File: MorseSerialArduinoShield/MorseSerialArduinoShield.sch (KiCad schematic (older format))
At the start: 13 parts, among them P1 Power, P2 Analog, P3 Digital, P4 Digital, P5 CONN_01X01, P6 CONN_01X01, P7 CONN_01X01, P8 CONN_01X01

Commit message: Organised project
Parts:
- added R? (x7): 1K, symbol Device:R
- R?: value R -> 1K
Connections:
- net at U?.1 (G): now also R?.1
- net at U?.10 (A): now also R?.1
- net at U?.2 (F): now also R?.1
- net at U?.4 (E): now also R?.1
- net at U?.5 (D): now also R?.1
- net at U?.6 (DP): now also R?.1
- net at U?.7 (C): now also R?.1
- net at U?.9 (B): now also R?.1
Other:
- note added: "pinMode(2, OUTPUT); // top right\n pinMode(4, OUTPUT); // top left\n pinMode(5, OUTPUT); // top centre\n pinMode(6, OUTPUT); // middle\n pinMode(7, OUTPUT); // Decimal point\n pinMode(8, OUTPUT); // bottom Right\n pinMode(10, OUTPUT); // bottom left\n pinMode(11, OUTPUT); // bottom\n pinMode(13, OUTPUT); // Buzzer"
- moved on the sheet: A?, BZ?, R?, RV?, U?
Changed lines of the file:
@@
 L Device:Buzzer BZ?
 U 1 1 5E8A2230
-P 4550 3100
-F 0 "BZ?" H 4702 3129 50  0000 L CNN
-F 1 "Buzzer" H 4702 3038 50  0000 L CNN
-F 2 "" V 4525 3200 50  0001 C CNN
-F 3 "~" V 4525 3200 50  0001 C CNN
-	1    4550 3100
-	1    0    0    -1
+P 4100 750
+F 0 "BZ?" H 4252 779 50  0000 L CNN
+F 1 "Buzzer" H 4252 688 50  0000 L CNN
+F 2 "" V 4075 850 50  0001 C CNN
+F 3 "~" V 4075 850 50  0001 C CNN
+	1    4100 750
+	0    -1   -1   0
 $EndComp
 $Comp
 L Display_Character:SC39-11SRWA U?
 U 1 1 5E8A0889
-P 4550 1850
-F 0 "U?" H 4550 2517 50  0000 C CNN
-F 1 "SC39-11SRWA" H 4550 2426 50  0000 C CNN
-F 2 "Display_7Segment:Sx39-1xxxxx" H 4550 1300 50  0001 C CNN
-F 3 "http://www.kingbrightusa.com/images/catalog/SPEC/sc39-11srwa.pdf" H 4550 1850 50  0001 C CNN
-	1    4550 1850
+P 4950 2300
+F 0 "U?" H 4950 2967 50  0000 C CNN
+F 1 "SC39-11SRWA" H 4950 2876 50  0000 C CNN
+F 2 "Display_7Segment:Sx39-1xxxxx" H 4950 1750 50  0001 C CNN
+F 3 "http://www.kingbrightusa.com/images/catalog/SPEC/sc39-11srwa.pdf" H 4950 2300 50  0001 C CNN
+	1    4950 2300
 	1    0    0    -1
 $EndComp
@@
 L Device:R R?
 U 1 1 5E8A1C48
-P 5600 2450
-F 0 "R?" H 5670 2496 50  0000 L CNN
-F 1 "R" H 5670 2405 50  0000 L CNN
-F 2 "" V 5530 2450 50  0001 C CNN
-F 3 "~" H 5600 2450 50  0001 C CNN
-	1    5600 2450
-	1    0    0    -1
+P 4500 2700
+F 0 "R?" H 4570 2746 50  0000 L CNN
+F 1 "1K" H 4570 2655 50  0000 L CNN
+F 2 "" V 4430 2700 50  0001 C CNN
+F 3 "~" H 4500 2700 50  0001 C CNN
+	1    4500 2700
+	0    1    1    0
 $EndComp
 $Comp
 L Device:R_POT_TRIM RV?
 U 1 1 5E8A2359
-P 5650 1150
-F 0 "RV?" H 5580 1196 50  0000 R CNN
-F 1 "R_POT_TRIM" H 5580 1105 50  0000 R CNN
-F 2 "" H 5650 1150 50  0001 C CNN
-F 3 "~" H 5650 1150 50  0001 C CNN
-	1    5650 1150
-	1    0    0    -1
+P 4550 900
+F 0 "RV?" H 4480 946 50  0000 R CNN
+F 1 "R_POT_TRIM" H 4480 855 50  0000 R CNN
+F 2 "" H 4550 900 50  0001 C CNN
+F 3 "~" H 4550 900 50  0001 C CNN
+	1    4550 900
+	0    1    1    0
 $EndComp
 $Comp
@@
 F 3 "https://www.arduino.cc/en/Main/arduinoBoardUno" H 3150 2400 50  0001 C CNN
 	1    3150 2400
-	1    0    0    -1
+	-1   0    0    1
 $EndComp
+$Comp
+L Device:R R?
+U 1 1 5ECADC31
+P 4500 2600
+F 0 "R?" H 4570 2646 50  0000 L CNN
+F 1 "1K" H 4570 2555 50  0000 L CNN
+F 2 "" V 4430 2600 50  0001 C CNN
+F 3 "~" H 4500 2600 50  0001 C CNN
+	1    4500 2600
+	0    1    1    0
+$EndComp
+$Comp
+L Device:R R?
+U 1 1 5ECAE2EE
+P 4500 2500
+F 0 "R?" H 4570 2546 50  0000 L CNN
+F 1 "1K" H 4570 2455 50  0000 L CNN
+F 2 "" V 4430 2500 50  0001 C CNN
+F 3 "~" H 4500 2500 50  0001 C CNN
+	1    4500 2500
+	0    1    1    0
+$EndComp
+$Comp
+L Device:R R?
+U 1 1 5ECAE473
+P 4500 2400
+F 0 "R?" H 4570 2446 50  0000 L CNN
+F 1 "1K" H 4570 2355 50  0000 L CNN
+F 2 "" V 4430 2400 50  0001 C CNN
+F 3 "~" H 4500 2400 50  0001 C CNN
+	1    4500 2400
+	0    1    1    0
+$EndComp
+$Comp
+L Device:R R?
+U 1 1 5ECAE650
+P 4500 2300
+F 0 "R?" H 4570 2346 50  0000 L CNN
+F 1 "1K" H 4570 2255 50  0000 L CNN
+F 2 "" V 4430 2300 50  0001 C CNN
+F 3 "~" H 4500 2300 50  0001 C CNN
+	1    4500 2300
+	0    1    1    0
+$EndComp
+$Comp
+L Device:R R?
+U 1 1 5ECAE844
+P 4500 2200
+F 0 "R?" H 4570 2246 50  0000 L CNN
+F 1 "1K" H 4570 2155 50  0000 L CNN
+F 2 "" V 4430 2200 50  0001 C CNN
+F 3 "~" H 4500 2200 50  0001 C CNN
+	1    4500 2200
+	0    1    1    0
+$EndComp
+$Comp
+L Device:R R?
+U 1 1 5ECAEC2F
+P 4500 2100
+F 0 "R?" H 4570 2146 50  0000 L CNN
+F 1 "1K" H 4570 2055 50  0000 L CNN
+F 2 "" V 4430 2100 50  0001 C CNN
+F 3 "~" H 4500 2100 50  0001 C CNN
+	1    4500 2100
+	0    1    1    0
+$EndComp
+$Comp
+L Device:R R?
+U 1 1 5ECAEFA7
+P 4500 2000
+F 0 "R?" H 4570 2046 50  0000 L CNN
+F 1 "1K" H 4570 1955 50  0000 L CNN
+F 2 "" V 4430 2000 50  0001 C CNN
+F 3 "~" H 4500 2000 50  0001 C CNN
+	1    4500 2000
+	0    1    1    0
+$EndComp
+Text Notes 4600 4100 0    50   ~ 0
+  pinMode(2, OUTPUT); // top right\n  pinMode(4, OUTPUT); // top left\n  pinMode(5, OUTPUT); // top centre\n  pinMode(6, OUTPUT); // middle\n  pinMode(7, OUTPUT); // Decimal point\n  pinMode(8, OUTPUT); // bottom Right\n  pinMode(10, OUTPUT); // bottom left\n  pinMode(11, OUTPUT);  // bottom\n  pinMode(13, OUTPUT); // Buzzer
 $EndSCHEMATC

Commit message: base line wiring
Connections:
- net at U?.3 (CC): now also A?.29 (GND), BZ?.2 (+)
- net at R?.2: now also A?.22 (D7)
- net at BZ?.1 (-): now also RV?.1
- net at RV?.2: now also A?.28 (D13), RV?.3
- net at A?.17 (D2): now also R?.2
- net at A?.19 (D4): now also R?.2
- net at A?.20 (D5): now also R?.2
- net at A?.21 (D6): now also R?.2
- net at A?.23 (D8): now also R?.2
- net at A?.25 (D10): now also R?.2
- net at A?.26 (D11): now also R?.2
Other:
- moved on the sheet: BZ?, RV?
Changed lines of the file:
@@
 L Device:Buzzer BZ?
 U 1 1 5E8A2230
-P 4100 750
-F 0 "BZ?" H 4252 779 50  0000 L CNN
-F 1 "Buzzer" H 4252 688 50  0000 L CNN
-F 2 "" V 4075 850 50  0001 C CNN
-F 3 "~" V 4075 850 50  0001 C CNN
-	1    4100 750
+P 4750 1450
+F 0 "BZ?" H 4902 1479 50  0000 L CNN
+F 1 "Buzzer" H 4902 1388 50  0000 L CNN
+F 2 "" V 4725 1550 50  0001 C CNN
+F 3 "~" V 4725 1550 50  0001 C CNN
+	1    4750 1450
 	0    -1   -1   0
 $EndComp
@@
 $EndComp
 $Comp
-L Device:R_POT_TRIM RV?
-U 1 1 5E8A2359
-P 4550 900
-F 0 "RV?" H 4480 946 50  0000 R CNN
-F 1 "R_POT_TRIM" H 4480 855 50  0000 R CNN
-F 2 "" H 4550 900 50  0001 C CNN
-F 3 "~" H 4550 900 50  0001 C CNN
-	1    4550 900
-	0    1    1    0
-$EndComp
+L Device:R R?
+U 1 1 5ECADC31
+P 4500 2600
+F 0 "R?" H 4570 2646 50  0000 L CNN
+F 1 "1K" H 4570 2555 50  0000 L CNN
+F 2 "" V 4430 2600 50  0001 C CNN
+F 3 "~" H 4500 2600 50  0001 C CNN
+	1    4500 2600
+	0    1    1    0
+$EndComp
+$Comp
+L Device:R R?
+U 1 1 5ECAE2EE
+P 4500 2500
+F 0 "R?" H 4570 2546 50  0000 L CNN
+F 1 "1K" H 4570 2455 50  0000 L CNN
+F 2 "" V 4430 2500 50  0001 C CNN
+F 3 "~" H 4500 2500 50  0001 C CNN
+	1    4500 2500
+	0    1    1    0
+$EndComp
+$Comp
+L Device:R R?
+U 1 1 5ECAE473
+P 4500 2400
+F 0 "R?" H 4570 2446 50  0000 L CNN
+F 1 "1K" H 4570 2355 50  0000 L CNN
+F 2 "" V 4430 2400 50  0001 C CNN
+F 3 "~" H 4500 2400 50  0001 C CNN
+	1    4500 2400
+	0    1    1    0
+$EndComp
+$Comp
+L Device:R R?
+U 1 1 5ECAE650
+P 4500 2300
+F 0 "R?" H 4570 2346 50  0000 L CNN
+F 1 "1K" H 4570 2255 50  0000 L CNN
+F 2 "" V 4430 2300 50  0001 C CNN
+F 3 "~" H 4500 2300 50  0001 C CNN
+	1    4500 2300
+	0    1    1    0
+$EndComp
+$Comp
+L Device:R R?
+U 1 1 5ECAE844
+P 4500 2200
+F 0 "R?" H 4570 2246 50  0000 L CNN
+F 1 "1K" H 4570 2155 50  0000 L CNN
+F 2 "" V 4430 2200 50  0001 C CNN
+F 3 "~" H 4500 2200 50  0001 C CNN
+	1    4500 2200
+	0    1    1    0
+$EndComp
+$Comp
+L Device:R R?
+U 1 1 5ECAEC2F
+P 4500 2100
+F 0 "R?" H 4570 2146 50  0000 L CNN
+F 1 "1K" H 4570 2055 50  0000 L CNN
+F 2 "" V 4430 2100 50  0001 C CNN
+F 3 "~" H 4500 2100 50  0001 C CNN
+	1    4500 2100
+	0    1    1    0
+$EndComp
+$Comp
+L Device:R R?
+U 1 1 5ECAEFA7
+P 4500 2000
+F 0 "R?" H 4570 2046 50  0000 L CNN
+F 1 "1K" H 4570 1955 50  0000 L CNN
+F 2 "" V 4430 2000 50  0001 C CNN
+F 3 "~" H 4500 2000 50  0001 C CNN
+	1    4500 2000
+	0    1    1    0
+$EndComp
+Text Notes 4600 4100 0    50   ~ 0
+  pinMode(2, OUTPUT); // top right\n  pinMode(4, OUTPUT); // top left\n  pinMode(5, OUTPUT); // top centre\n  pinMode(6, OUTPUT); // middle\n  pinMode(7, OUTPUT); // Decimal point\n  pinMode(8, OUTPUT); // bottom Right\n  pinMode(10, OUTPUT); // bottom left\n  pinMode(11, OUTPUT);  // bottom\n  pinMode(13, OUTPUT); // Buzzer
+Entry Wire Line
+	4550 2400 4650 2500
 $Comp
 L MCU_Module:Arduino_UNO_R3 A?
@@
 	-1   0    0    1
 $EndComp
-$Comp
-L Device:R R?
-U 1 1 5ECADC31
-P 4500 2600
-F 0 "R?" H 4570 2646 50  0000 L CNN
-F 1 "1K" H 4570 2555 50  0000 L CNN
-F 2 "" V 4430 2600 50  0001 C CNN
-F 3 "~" H 4500 2600 50  0001 C CNN
-	1    4500 2600
-	0    1    1    0
-$EndComp
-$Comp
-L Device:R R?
-U 1 1 5ECAE2EE
-P 4500 2500
-F 0 "R?" H 4570 2546 50  0000 L CNN
-F 1 "1K" H 4570 2455 50  0000 L CNN
-F 2 "" V 4430 2500 50  0001 C CNN
-F 3 "~" H 4500 2500 50  0001 C CNN
-	1    4500 2500
-	0    1    1    0
-$EndComp
-$Comp
-L Device:R R?
-U 1 1 5ECAE473
-P 4500 2400
-F 0 "R?" H 4570 2446 50  0000 L CNN
-F 1 "1K" H 4570 2355 50  0000 L CNN
-F 2 "" V 4430 2400 50  0001 C CNN
-F 3 "~" H 4500 2400 50  0001 C CNN
-	1    4500 2400
-	0    1    1    0
-$EndComp
-$Comp
-L Device:R R?
-U 1 1 5ECAE650
-P 4500 2300
-F 0 "R?" H 4570 2346 50  0000 L CNN
-F 1 "1K" H 4570 2255 50  0000 L CNN
-F 2 "" V 4430 2300 50  0001 C CNN
-F 3 "~" H 4500 2300 50  0001 C CNN
-	1    4500 2300
-	0    1    1    0
-$EndComp
-$Comp
-L Device:R R?
-U 1 1 5ECAE844
-P 4500 2200
-F 0 "R?" H 4570 2246 50  0000 L CNN
-F 1 "1K" H 4570 2155 50  0000 L CNN
-F 2 "" V 4430 2200 50  0001 C CNN
-F 3 "~" H 4500 2200 50  0001 C CNN
-	1    4500 2200
-	0    1    1    0
-$EndComp
-$Comp
-L Device:R R?
-U 1 1 5ECAEC2F
-P 4500 2100
-F 0 "R?" H 4570 2146 50  0000 L CNN
-F 1 "1K" H 4570 2055 50  0000 L CNN
-F 2 "" V 4430 2100 50  0001 C CNN
-F 3 "~" H 4500 2100 50  0001 C CNN
-	1    4500 2100
-	0    1    1    0
-$EndComp
-$Comp
-L Device:R R?
-U 1 1 5ECAEFA7
-P 4500 2000
-F 0 "R?" H 4570 2046 50  0000 L CNN
-F 1 "1K" H 4570 1955 50  0000 L CNN
-F 2 "" V 4430 2000 50  0001 C CNN
-F 3 "~" H 4500 2000 50  0001 C CNN
-	1    4500 2000
-	0    1    1    0
-$EndComp
-Text Notes 4600 4100 0    50   ~ 0
-  pinMode(2, OUTPUT); // top right\n  pinMode(4, OUTPUT); // top left\n  pinMode(5, OUTPUT); // top centre\n  pinMode(6, OUTPUT); // middle\n  pinMode(7, OUTPUT); // Decimal point\n  pinMode(8, OUTPUT); // bottom Right\n  pinMode(10, OUTPUT); // bottom left\n  pinMode(11, OUTPUT);  // bottom\n  pinMode(13, OUTPUT); // Buzzer
+Wire Wire Line
+	4250 1550 4650 1550
+$Comp
+L Device:R_POT_TRIM RV?
+U 1 1 5E8A2359
+P 4100 1550
+F 0 "RV?" H 4030 1596 50  0000 R CNN
+F 1 "R_POT_TRIM" H 4030 1505 50  0000 R CNN
+F 2 "" H 4100 1550 50  0001 C CNN
+F 3 "~" H 4100 1550 50  0001 C CNN
+	1    4100 1550
+	0    1    1    0
+$EndComp
+Wire Wire Line
+	3650 1700 3650 1550
+Wire Wire Line
+	3650 1550 3950 1550
+Wire Wire Line
+	3650 1700 4100 1700
+Connection ~ 3650 1700
+Wire Wire Line
+	3250 1300 3250 900
+Wire Wire Line
+	3250 900  5250 900
+Wire Wire Line
+	5250 900  5250 1550
+Wire Wire Line
+	4850 1550 5250 1550
+Connection ~ 5250 1550
+Wire Wire Line
+	5250 1550 5250 2600
+Wire Wire Line
+	4050 2800 4050 2100
+Wire Wire Line
+	4050 2100 4350 2100
+Wire Wire Line
+	3650 2800 4050 2800
+Wire Wire Line
+	4200 2500 4350 2500
+Wire Wire Line
+	3650 2500 4000 2500
+Wire Wire Line
+	4000 2500 4000 2000
+Wire Wire Line
+	3650 2600 4200 2600
+Wire Wire Line
+	3650 2400 4250 2400
+Wire Wire Line
+	4250 2400 4250 2600
+Wire Wire Line
+	4250 2600 4350 2600
+Wire Wire Line
+	4200 2600 4200 2500
+Wire Wire Line
+	3650 2300 4150 2300
+Wire Wire Line
+	4150 2300 4150 2700
+Wire Wire Line
+	4150 2700 4350 2700
+Wire Wire Line
+	3650 2200 4350 2200
+Wire Wire Line
+	4000 2000 4350 2000
+Wire Wire Line
+	3650 2000 3900 2000
+Wire Wire Line
+	3900 2000 3900 1950
+Wire Wire Line
+	3900 1950 4300 1950
+Wire Wire Line
+	4300 1950 4300 2400
+Wire Wire Line
+	4300 2400 4350 2400
+Wire Wire Line
+	3650 1900 4350 1900
+Wire Wire Line
+	4350 1900 4350 2300
 $EndSCHEMATC

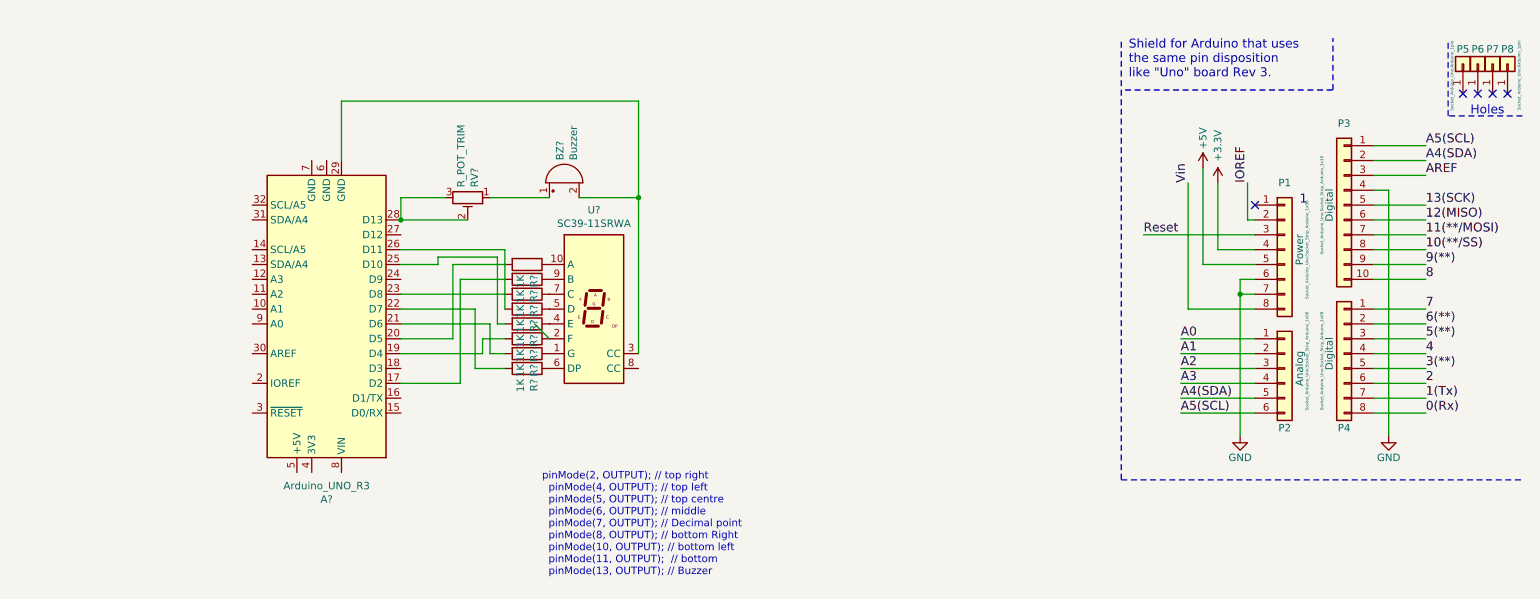
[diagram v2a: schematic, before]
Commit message: Removal of ardinuo template stuff
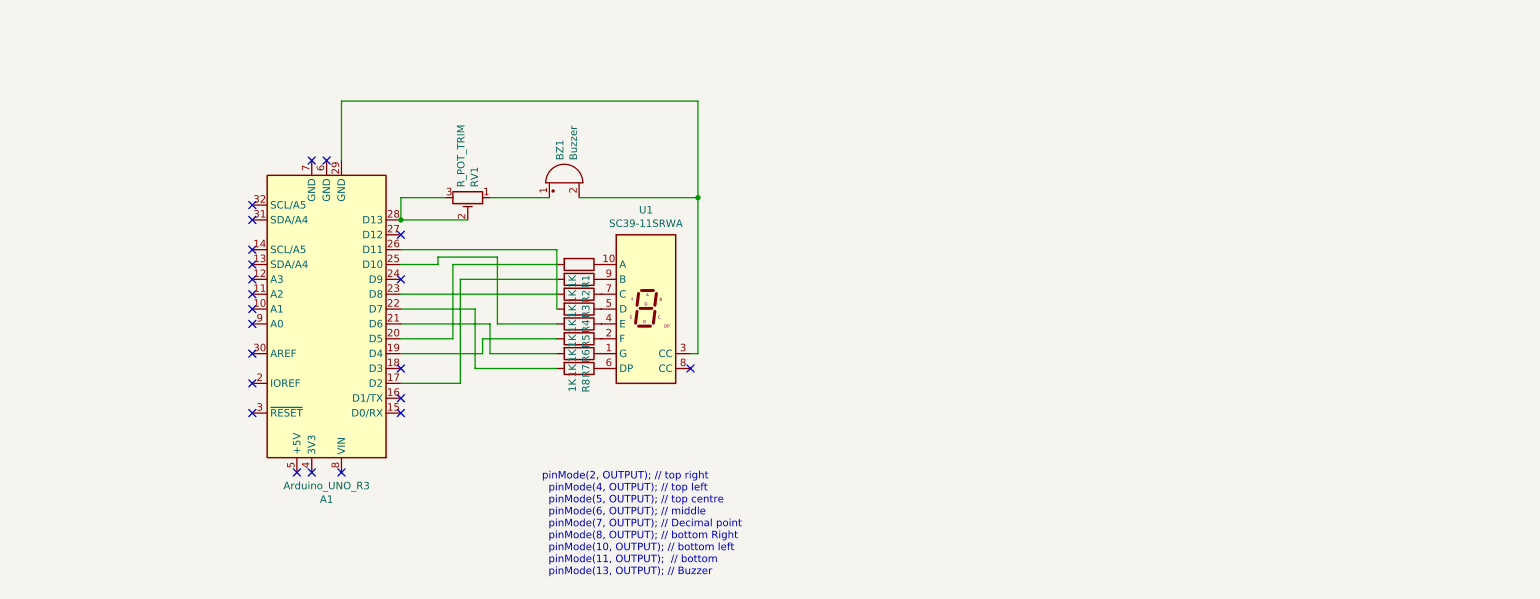
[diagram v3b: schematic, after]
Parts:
- removed P1: Power, Socket_Arduino_Uno:Socket_Strip_Arduino_1x08, symbol Connector_Generic:Conn_01x08
- removed P2: Analog, Socket_Arduino_Uno:Socket_Strip_Arduino_1x06, symbol Connector_Generic:Conn_01x06
- removed P3: Digital, Socket_Arduino_Uno:Socket_Strip_Arduino_1x10, symbol Connector_Generic:Conn_01x10
- removed P4: Digital, Socket_Arduino_Uno:Socket_Strip_Arduino_1x08, symbol Connector_Generic:Conn_01x08
- removed P5, P6, P7, P8: CONN_01X01, Socket_Arduino_Uno:Arduino_1pin, symbol Connector_Generic:Conn_01x01
- gave numbers to parts that had none: 12
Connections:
- no-connect marks 5 -> 22
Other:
- note removed: "1"
- note removed: "Holes"
- note removed: "Shield for Arduino that uses\nthe same pin disposition\nlike "Uno" board Rev 3."
- moved on the sheet: R1, R2, R3, R4, R5, R6, R7, R8, U1

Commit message: ERC rules worrk
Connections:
- net GND: now reaches A1.29 (GND), BZ1.2 (+), U1.3 (CC)
- no-connect marks 22 -> 21
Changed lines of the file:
@@
 NoConn ~ 2650 1700
 NoConn ~ 2650 1600
-NoConn ~ 3050 1300
-NoConn ~ 3150 1300
 Wire Wire Line
 	3250 900  3250 1300
-NoConn ~ 3250 3400
+$Comp
+L power:PWR_FLAG #FLG0101
+U 1 1 5EE02302
+P 3300 3950
+F 0 "#FLG0101" H 3300 4025 50  0001 C CNN
+F 1 "PWR_FLAG" H 3300 4123 50  0000 C CNN
+F 2 "" H 3300 3950 50  0001 C CNN
+F 3 "~" H 3300 3950 50  0001 C CNN
+	1    3300 3950
+	-1   0    0    1
+$EndComp
+Wire Wire Line
+	3250 3400 3250 3950
+Wire Wire Line
+	3250 3950 3300 3950
+NoConn ~ 3150 1300
+NoConn ~ 3050 1300
+$Comp
+L power:GND #PWR0101
+U 1 1 5EE065B4
+P 2100 950
+F 0 "#PWR0101" H 2100 700 50  0001 C CNN
+F 1 "GND" H 2105 777 50  0000 C CNN
+F 2 "" H 2100 950 50  0001 C CNN
+F 3 "" H 2100 950 50  0001 C CNN
+	1    2100 950
+	1    0    0    -1
+$EndComp
+$Comp
+L power:PWR_FLAG #FLG0102
+U 1 1 5EE06DA0
+P 2100 700
+F 0 "#FLG0102" H 2100 775 50  0001 C CNN
+F 1 "PWR_FLAG" H 2100 873 50  0000 C CNN
+F 2 "" H 2100 700 50  0001 C CNN
+F 3 "~" H 2100 700 50  0001 C CNN
+	1    2100 700
+	1    0    0    -1
+$EndComp
+Wire Wire Line
+	2100 700  2100 950
+$Comp
+L power:PWR_FLAG #FLG0103
+U 1 1 5EE091E9
+P 1250 850
+F 0 "#FLG0103" H 1250 925 50  0001 C CNN
+F 1 "PWR_FLAG" H 1250 1023 50  0000 C CNN
+F 2 "" H 1250 850 50  0001 C CNN
+F 3 "~" H 1250 850 50  0001 C CNN
+	1    1250 850
+	1    0    0    -1
+$EndComp
+$Comp
+L power:+5V #PWR0102
+U 1 1 5EE09EFF
+P 1250 1200
+F 0 "#PWR0102" H 1250 1050 50  0001 C CNN
+F 1 "+5V" H 1265 1373 50  0000 C CNN
+F 2 "" H 1250 1200 50  0001 C CNN
+F 3 "" H 1250 1200 50  0001 C CNN
+	1    1250 1200
+	-1   0    0    1
+$EndComp
+Wire Wire Line
+	1250 850  1250 1200
+$Comp
+L power:GND #PWR0103
+U 1 1 5EE0BAD3
+P 3250 850
+F 0 "#PWR0103" H 3250 600 50  0001 C CNN
+F 1 "GND" H 3255 677 50  0000 C CNN
+F 2 "" H 3250 850 50  0001 C CNN
+F 3 "" H 3250 850 50  0001 C CNN
+	1    3250 850
+	-1   0    0    1
+$EndComp
+Wire Wire Line
+	3250 850  3250 900
+Connection ~ 3250 900
 $EndSCHEMATC

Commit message: pre pcb design
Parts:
- BZ1: footprint (none) -> Buzzer_Beeper:Buzzer_15x7.5RM7.6
- R1, R2, R3, R4, R5, R6, R7, R8: footprint (none) -> Resistor_THT:R_Axial_DIN0309_L9.0mm_D3.2mm_P12.70mm_Horizontal
- RV1: footprint (none) -> Potentiometer_THT:Potentiometer_Piher_PT-15-V15_Vertical
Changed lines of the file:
@@
 F 0 "BZ1" H 4902 1479 50  0000 L CNN
 F 1 "Buzzer" H 4902 1388 50  0000 L CNN
-F 2 "" V 4725 1550 50  0001 C CNN
+F 2 "Buzzer_Beeper:Buzzer_15x7.5RM7.6" V 4725 1550 50  0001 C CNN
 F 3 "~" V 4725 1550 50  0001 C CNN
 	1    4750 1450
@@
 F 0 "R8" H 4920 2746 50  0000 L CNN
 F 1 "1K" H 4920 2655 50  0000 L CNN
-F 2 "" V 4780 2700 50  0001 C CNN
+F 2 "Resistor_THT:R_Axial_DIN0309_L9.0mm_D3.2mm_P12.70mm_Horizontal" V 4780 2700 50  0001 C CNN
 F 3 "~" H 4850 2700 50  0001 C CNN
 	1    4850 2700
@@
 F 0 "R7" H 4920 2646 50  0000 L CNN
 F 1 "1K" H 4920 2555 50  0000 L CNN
-F 2 "" V 4780 2600 50  0001 C CNN
+F 2 "Resistor_THT:R_Axial_DIN0309_L9.0mm_D3.2mm_P12.70mm_Horizontal" V 4780 2600 50  0001 C CNN
 F 3 "~" H 4850 2600 50  0001 C CNN
 	1    4850 2600
@@
 F 0 "R6" H 4920 2546 50  0000 L CNN
 F 1 "1K" H 4920 2455 50  0000 L CNN
-F 2 "" V 4780 2500 50  0001 C CNN
+F 2 "Resistor_THT:R_Axial_DIN0309_L9.0mm_D3.2mm_P12.70mm_Horizontal" V 4780 2500 50  0001 C CNN
 F 3 "~" H 4850 2500 50  0001 C CNN
 	1    4850 2500
@@
 F 0 "R5" H 4920 2446 50  0000 L CNN
 F 1 "1K" H 4920 2355 50  0000 L CNN
-F 2 "" V 4780 2400 50  0001 C CNN
+F 2 "Resistor_THT:R_Axial_DIN0309_L9.0mm_D3.2mm_P12.70mm_Horizontal" V 4780 2400 50  0001 C CNN
 F 3 "~" H 4850 2400 50  0001 C CNN
 	1    4850 2400
@@
 F 0 "R4" H 4920 2346 50  0000 L CNN
 F 1 "1K" H 4920 2255 50  0000 L CNN
-F 2 "" V 4780 2300 50  0001 C CNN
+F 2 "Resistor_THT:R_Axial_DIN0309_L9.0mm_D3.2mm_P12.70mm_Horizontal" V 4780 2300 50  0001 C CNN
 F 3 "~" H 4850 2300 50  0001 C CNN
 	1    4850 2300
@@
 F 0 "R3" H 4920 2246 50  0000 L CNN
 F 1 "1K" H 4920 2155 50  0000 L CNN
-F 2 "" V 4780 2200 50  0001 C CNN
+F 2 "Resistor_THT:R_Axial_DIN0309_L9.0mm_D3.2mm_P12.70mm_Horizontal" V 4780 2200 50  0001 C CNN
 F 3 "~" H 4850 2200 50  0001 C CNN
 	1    4850 2200
@@
 F 0 "R2" H 4920 2146 50  0000 L CNN
 F 1 "1K" H 4920 2055 50  0000 L CNN
-F 2 "" V 4780 2100 50  0001 C CNN
+F 2 "Resistor_THT:R_Axial_DIN0309_L9.0mm_D3.2mm_P12.70mm_Horizontal" V 4780 2100 50  0001 C CNN
 F 3 "~" H 4850 2100 50  0001 C CNN
 	1    4850 2100
@@
 F 0 "RV1" H 4030 1596 50  0000 R CNN
 F 1 "R_POT_TRIM" H 4030 1505 50  0000 R CNN
-F 2 "" H 4100 1550 50  0001 C CNN
+F 2 "Potentiometer_THT:Potentiometer_Piher_PT-15-V15_Vertical" H 4100 1550 50  0001 C CNN
 F 3 "~" H 4100 1550 50  0001 C CNN
 	1    4100 1550
@@
 F 0 "R1" H 4920 2046 50  0000 L CNN
 F 1 "1K" H 4920 1955 50  0000 L CNN
-F 2 "" V 4780 2000 50  0001 C CNN
+F 2 "Resistor_THT:R_Axial_DIN0309_L9.0mm_D3.2mm_P12.70mm_Horizontal" V 4780 2000 50  0001 C CNN
 F 3 "~" H 4850 2000 50  0001 C CNN
 	1    4850 2000

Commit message: BaseLine PCB design
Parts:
- RV1: footprint Potentiometer_THT:Potentiometer_Piher_PT-15-V15_Vertical -> Potentiometer_THT:Potentiometer_Runtron_RM-065_Vertical
- U1: footprint Display_7Segment:Sx39-1xxxxx -> Display_7Segment:7SegmentLED_LTS6760_LTS6780
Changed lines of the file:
@@
 F 0 "RV1" H 4030 1596 50  0000 R CNN
 F 1 "R_POT_TRIM" H 4030 1505 50  0000 R CNN
-F 2 "Potentiometer_THT:Potentiometer_Piher_PT-15-V15_Vertical" H 4100 1550 50  0001 C CNN
+F 2 "Potentiometer_THT:Potentiometer_Runtron_RM-065_Vertical" H 4100 1550 50  0001 C CNN
 F 3 "~" H 4100 1550 50  0001 C CNN
 	1    4100 1550
@@
 F 0 "U1" H 5300 2967 50  0000 C CNN
 F 1 "SC39-11SRWA" H 5300 2876 50  0000 C CNN
-F 2 "Display_7Segment:Sx39-1xxxxx" H 5300 1750 50  0001 C CNN
+F 2 "Display_7Segment:7SegmentLED_LTS6760_LTS6780" H 5300 1750 50  0001 C CNN
 F 3 "http://www.kingbrightusa.com/images/catalog/SPEC/sc39-11srwa.pdf" H 5300 2300 50  0001 C CNN
 	1    5300 2300

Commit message: startpoint
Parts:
- BZ1: footprint Buzzer_Beeper:Buzzer_15x7.5RM7.6 -> Buzzer_Beeper:Buzzer_12x9.5RM7.6
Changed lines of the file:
@@
 F 0 "BZ1" H 4902 1479 50  0000 L CNN
 F 1 "Buzzer" H 4902 1388 50  0000 L CNN
-F 2 "Buzzer_Beeper:Buzzer_15x7.5RM7.6" V 4725 1550 50  0001 C CNN
+F 2 "Buzzer_Beeper:Buzzer_12x9.5RM7.6" V 4725 1550 50  0001 C CNN
 F 3 "~" V 4725 1550 50  0001 C CNN
 	1    4750 1450
